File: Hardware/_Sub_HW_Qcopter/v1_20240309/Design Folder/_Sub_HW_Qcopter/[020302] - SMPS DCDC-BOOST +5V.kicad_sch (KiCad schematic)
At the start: 11 parts, among them U3902 TPS613222ADBVR

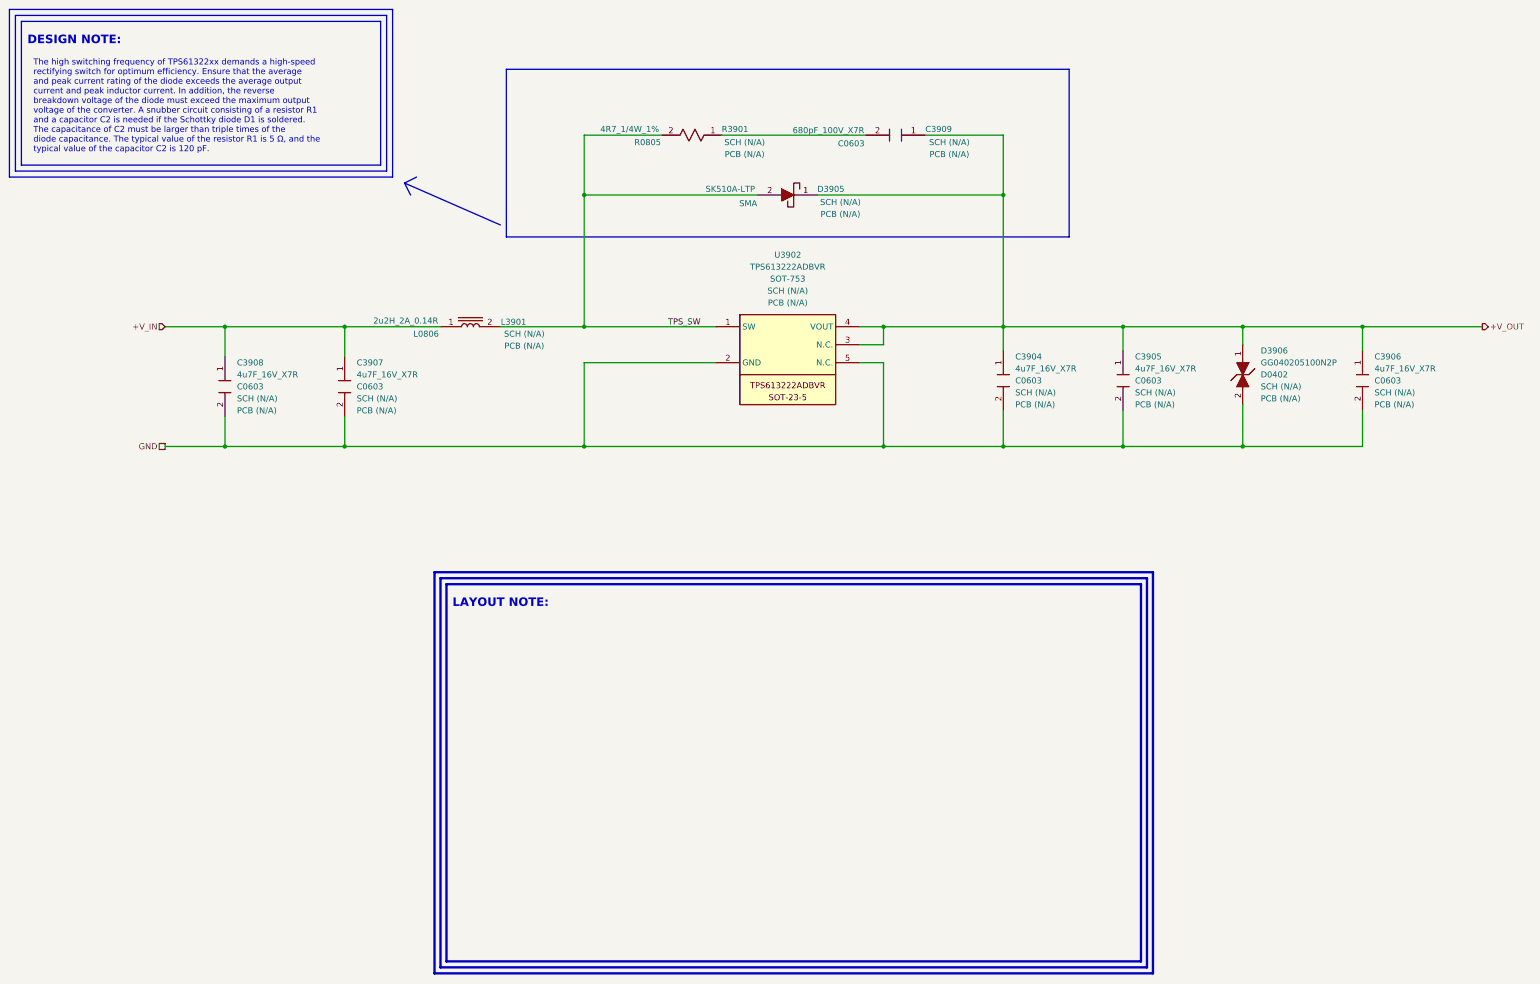
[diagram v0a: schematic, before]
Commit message: Update [020302] - SMPS DCDC-BOOST +5V.kicad_sch
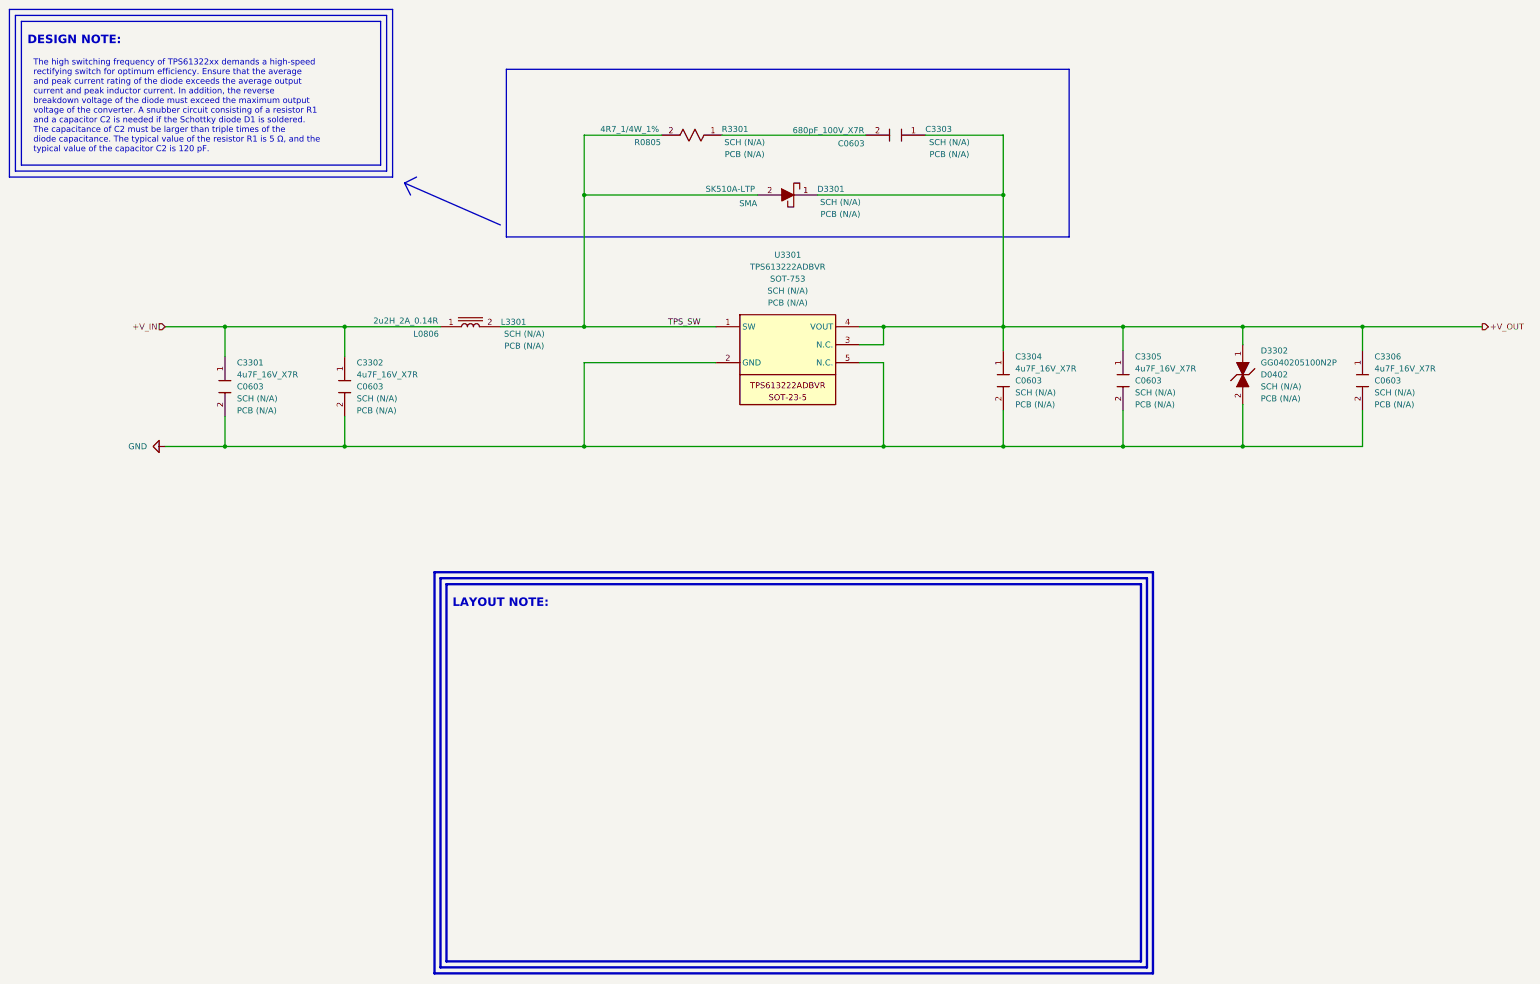
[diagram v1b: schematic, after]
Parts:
- renumbered C3908 to C3301, C3907 to C3302, C3909 to C3303, C3904 to C3304, C3905 to C3305, C3906 to C3306, D3905 to D3301, D3906 to D3302, L3901 to L3301, R3901 to R3301, U3902 to U3301
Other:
- company: (none) -> Mend0z0
- title: (none) -> Quadcopter
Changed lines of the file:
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@@
 	(paper "C")
 	(title_block
-		(comment 2 "DRAFT")
+		(title "Quadcopter")
+		(date "2024-03-17")
+		(rev "01")
+		(company "Mend0z0")
+		(comment 1 "01")
+		(comment 2 "PRELIMINARY")
+		(comment 3 "Siavash Taher Parvar")
+		(comment 8 "N/A")
+		(comment 9 "First Version")
 	)
 	(junction
@@
 		)
 	)
-	(hierarchical_label "GND"
-		(shape passive)
-		(at 139.7 228.6 180)
-		(fields_autoplaced yes)
-		(effects
-			(font
-				(size 1.27 1.27)
-			)
-			(justify right)
-		)
-	)
 	(hierarchical_label "+V_IN"
 		(shape input)
@@
 		(on_board yes)
 		(dnp no)
-		(property "Reference" "C3909"
+		(property "Reference" "C3303"
 			(at 303.784 161.29 0)
 			(effects
@@
 			(project "_Sub_HW_Qcopter"
 				(path "/b8703f06-b3da-4de2-b217-f104939b36e8/6184e84e-040e-4878-8152-76cf0b949e21/0ce565c6-f8fe-4174-9716-15fae563dcc2/86512584-84de-43e1-b652-f4f460ec7f16"
-					(reference "C3909")
+					(reference "C3303")
 					(unit 1)
 				)
@@
 		(on_board yes)
 		(dnp no)
-		(property "Reference" "L3901"
+		(property "Reference" "L3301"
 			(at 213.614 202.184 0)
 			(effects
@@
 			(project "_Sub_HW_Qcopter"
 				(path "/b8703f06-b3da-4de2-b217-f104939b36e8/6184e84e-040e-4878-8152-76cf0b949e21/0ce565c6-f8fe-4174-9716-15fae563dcc2/86512584-84de-43e1-b652-f4f460ec7f16"
-					(reference "L3901")
+					(reference "L3301")
 					(unit 1)
 				)
@@
 		(dnp no)
 		(fields_autoplaced yes)
-		(property "Reference" "C3908"
+		(property "Reference" "C3301"
 			(at 154.94 210.8199 90)
 			(effects
@@
 			(project "_Sub_HW_Qcopter"
 				(path "/b8703f06-b3da-4de2-b217-f104939b36e8/6184e84e-040e-4878-8152-76cf0b949e21/0ce565c6-f8fe-4174-9716-15fae563dcc2/86512584-84de-43e1-b652-f4f460ec7f16"
-					(reference "C3908")
+					(reference "C3301")
 					(unit 1)
 				)
@@
 		(on_board yes)
 		(dnp no)
-		(property "Reference" "R3901"
+		(property "Reference" "R3301"
 			(at 260.604 161.29 0)
 			(effects
@@
 			(project "_Sub_HW_Qcopter"
 				(path "/b8703f06-b3da-4de2-b217-f104939b36e8/6184e84e-040e-4878-8152-76cf0b949e21/0ce565c6-f8fe-4174-9716-15fae563dcc2/86512584-84de-43e1-b652-f4f460ec7f16"
-					(reference "R3901")
+					(reference "R3301")
 					(unit 1)
 				)
@@
 		(dnp no)
 		(fields_autoplaced yes)
-		(property "Reference" "C3907"
+		(property "Reference" "C3302"
 			(at 180.34 210.8199 90)
 			(effects
@@
 			(project "_Sub_HW_Qcopter"
 				(path "/b8703f06-b3da-4de2-b217-f104939b36e8/6184e84e-040e-4878-8152-76cf0b949e21/0ce565c6-f8fe-4174-9716-15fae563dcc2/86512584-84de-43e1-b652-f4f460ec7f16"
-					(reference "C3907")
+					(reference "C3302")
 					(unit 1)
 				)
@@
 		(on_board yes)
 		(dnp no)
-		(property "Reference" "D3905"
+		(property "Reference" "D3301"
 			(at 280.924 173.99 0)
 			(effects
@@
 			(project "_Sub_HW_Qcopter"
 				(path "/b8703f06-b3da-4de2-b217-f104939b36e8/6184e84e-040e-4878-8152-76cf0b949e21/0ce565c6-f8fe-4174-9716-15fae563dcc2/86512584-84de-43e1-b652-f4f460ec7f16"
-					(reference "D3905")
+					(reference "D3301")
+					(unit 1)
+				)
+			)
+		)
+	)
+	(symbol
+		(lib_id "power:GND")
+		(at 139.7 228.6 270)
+		(unit 1)
+		(exclude_from_sim no)
+		(in_bom yes)
+		(on_board yes)
+		(dnp no)
+		(fields_autoplaced yes)
+		(property "Reference" "#PWR03301"
+			(at 133.35 228.6 0)
+			(effects
+				(font
+					(size 1.27 1.27)
+				)
+				(hide yes)
+			)
+		)
+		(property "Value" "GND"
+			(at 135.89 228.5999 90)
+			(effects
+				(font
+					(size 1.27 1.27)
+				)
+				(justify right)
+			)
+		)
+		(property "Footprint" ""
+			(at 139.7 228.6 0)
+			(effects
+				(font
+					(size 1.27 1.27)
+				)
+				(hide yes)
+			)
+		)
+		(property "Datasheet" ""
+			(at 139.7 228.6 0)
+			(effects
+				(font
+					(size 1.27 1.27)
+				)
+				(hide yes)
+			)
+		)
+		(property "Description" "Power symbol creates a global label with name \"GND\" , ground"
+			(at 139.7 228.6 0)
+			(effects
+				(font
+					(size 1.27 1.27)
+				)
+				(hide yes)
+			)
+		)
+		(pin "1"
+		)
+		(instances
+			(project "_Sub_HW_Qcopter"
+				(path "/b8703f06-b3da-4de2-b217-f104939b36e8/6184e84e-040e-4878-8152-76cf0b949e21/0ce565c6-f8fe-4174-9716-15fae563dcc2/86512584-84de-43e1-b652-f4f460ec7f16"
+					(reference "#PWR03301")
 					(unit 1)
 				)
@@
 		(dnp no)
 		(fields_autoplaced yes)
-		(property "Reference" "C3904"
+		(property "Reference" "C3304"
 			(at 320.04 209.5499 90)
 			(effects
@@
 			(project "_Sub_HW_Qcopter"
 				(path "/b8703f06-b3da-4de2-b217-f104939b36e8/6184e84e-040e-4878-8152-76cf0b949e21/0ce565c6-f8fe-4174-9716-15fae563dcc2/86512584-84de-43e1-b652-f4f460ec7f16"
-					(reference "C3904")
+					(reference "C3304")
 					(unit 1)
 				)
@@
 		(dnp no)
 		(fields_autoplaced yes)
-		(property "Reference" "D3906"
+		(property "Reference" "D3302"
 			(at 372.11 208.2799 90)
 			(effects
@@
 			(project "_Sub_HW_Qcopter"
 				(path "/b8703f06-b3da-4de2-b217-f104939b36e8/6184e84e-040e-4878-8152-76cf0b949e21/0ce565c6-f8fe-4174-9716-15fae563dcc2/86512584-84de-43e1-b652-f4f460ec7f16"
-					(reference "D3906")
+					(reference "D3302")
 					(unit 1)
 				)
@@
 		(dnp no)
 		(fields_autoplaced yes)
-		(property "Reference" "C3905"
+		(property "Reference" "C3305"
 			(at 345.44 209.5499 90)
 			(effects
@@
 			(project "_Sub_HW_Qcopter"
 				(path "/b8703f06-b3da-4de2-b217-f104939b36e8/6184e84e-040e-4878-8152-76cf0b949e21/0ce565c6-f8fe-4174-9716-15fae563dcc2/86512584-84de-43e1-b652-f4f460ec7f16"
-					(reference "C3905")
+					(reference "C3305")
 					(unit 1)
 				)
@@
 		(dnp no)
 		(fields_autoplaced yes)
-		(property "Reference" "C3906"
+		(property "Reference" "C3306"
 			(at 396.24 209.5499 90)
 			(effects
@@
 			(project "_Sub_HW_Qcopter"
 				(path "/b8703f06-b3da-4de2-b217-f104939b36e8/6184e84e-040e-4878-8152-76cf0b949e21/0ce565c6-f8fe-4174-9716-15fae563dcc2/86512584-84de-43e1-b652-f4f460ec7f16"
-					(reference "C3906")
+					(reference "C3306")
 					(unit 1)
 				)
@@
 		(dnp no)
 		(fields_autoplaced yes)
-		(property "Reference" "U3902"
+		(property "Reference" "U3301"
 			(at 271.78 187.96 0)
 			(effects
@@
 			(project "_Sub_HW_Qcopter"
 				(path "/b8703f06-b3da-4de2-b217-f104939b36e8/6184e84e-040e-4878-8152-76cf0b949e21/0ce565c6-f8fe-4174-9716-15fae563dcc2/86512584-84de-43e1-b652-f4f460ec7f16"
-					(reference "U3902")
+					(reference "U3301")
 					(unit 1)
 				)
